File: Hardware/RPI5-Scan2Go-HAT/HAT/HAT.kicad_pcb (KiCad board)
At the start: 2 copper layers, 76 x 96.5 mm, 39 parts, among them J1 RPi_GPIO, J10 Conn_01x02_Socket, J12 Conn_01x02_Socket, J13 Conn_01x02_Socket, J14 Conn_01x02_Socket, J15 Jack-DC 5V, J18 Conn_01x02_Socket, J19 Conn_01x02_Socket, J2 Conn_01x04_Socket, J20 Conn_01x05_Socket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

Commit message: minor improvements
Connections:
- J8 pad 1: /PICORST -> GND
- J8 pad 2: GND -> /PICORST
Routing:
- net /PICORST: track 42.0 -> 45.1 mm, vias 2 -> 3
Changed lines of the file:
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@@
 		(tags "TVS Diode (Uni-directional)")
 		(property "Reference" "D1"
-			(at 0 0 -90)
-			(layer "B.SilkS")
+			(at 0.1 2.9 90)
+			(layer "F.SilkS")
 			(effects
 				(font
-					(size 1.27 1.27)
-					(thickness 0.254)
+					(size 1 1)
+					(thickness 0.15)
 				)
-				(justify mirror)
 			)
 		)
@@
 			(remove_unused_layers no)
 			(roundrect_rratio 0.147059)
-			(net 5 "/PICORST")
+			(net 3 "GND")
 			(pinfunction "Pin_1")
 			(pintype "passive")
@@
 			(layers "*.Cu" "*.Mask")
 			(remove_unused_layers no)
-			(net 3 "GND")
+			(net 5 "/PICORST")
 			(pinfunction "Pin_2")
 			(pintype "passive")
@@
 		(tags "capacitor handsolder")
 		(property "Reference" "C1"
-			(at 0 -1.85 -180)
-			(layer "B.SilkS")
+			(at 0 -1.85 180)
+			(layer "F.SilkS")
 			(effects
 				(font
@@
 					(thickness 0.15)
 				)
-				(justify mirror)
 			)
 		)
@@
 		(tags "fuse handsolder")
 		(property "Reference" "F1"
-			(at 0 2.3 -270)
-			(layer "B.SilkS")
+			(at 0 2.3 270)
+			(layer "F.SilkS")
 			(effects
 				(font
@@
 					(thickness 0.15)
 				)
-				(justify mirror)
 			)
 		)
@@
 			(layer "F.SilkS")
 		)
-		(fp_poly
-			(pts
-				(xy 3.7 -20.2) (xy -3.7 -20.2) (xy -3.7 -24.9) (xy 3.7 -24.9)
-			)
-			(stroke
-				(width 0.1)
-				(type solid)
-			)
-			(fill solid)
-			(layer "Dwgs.User")
-		)
-		(fp_poly
-			(pts
-				(xy -1.5 -16.5) (xy -3.5 -16.5) (xy -3.5 -18.5) (xy -1.5 -18.5)
-			)
+		(fp_rect
+			(start -3.4544 -25.5016)
+			(end 3.7084 -20.4724)
 			(stroke
 				(width 0.1)
-				(type solid)
+				(type default)
 			)
-			(fill solid)
-			(layer "Dwgs.User")
+			(fill none)
+			(layer "F.SilkS")
+			(net 9)
 		)
-		(fp_poly
-			(pts
-				(xy -1.5 -14) (xy -3.5 -14) (xy -3.5 -16) (xy -1.5 -16)
-			)
+		(fp_rect
+			(start -1.6764 -25.0952)
+			(end -1.016 -24.2316)
 			(stroke
 				(width 0.1)
-				(type solid)
+				(type default)
 			)
-			(fill solid)
-			(layer "Dwgs.User")
+			(fill none)
+			(layer "F.SilkS")
+			(net 9)
 		)
-		(fp_poly
-			(pts
-				(xy -1.5 -11.5) (xy -3.5 -11.5) (xy -3.5 -13.5) (xy -1.5 -13.5)
-			)
+		(fp_rect
+			(start 1.3716 -25.0444)
+			(end 2.032 -24.1808)
 			(stroke
 				(width 0.1)
-				(type solid)
+				(type default)
 			)
-			(fill solid)
-			(layer "Dwgs.User")
+			(fill none)
+			(layer "F.SilkS")
 		)
 		(fp_line
@@
 			(layer "F.Fab")
 		)
-		(fp_text user "PICO"
-			(at -3.1 -1 90)
+		(fp_text user "USB"
+			(at -2.9464 -20.9296 90)
 			(unlocked yes)
 			(layer "F.SilkS")
@@
 				(font
 					(size 2 2)
-					(thickness 0.25)
+					(thickness 0.2)
 				)
 				(justify left bottom)
@@
 				(offset 0.31 -0.0694)
 			)
-			(layers "F.Cu" "F.Paste")
+			(layers "F.Cu" "F.Mask")
 			(net 80 "unconnected-(U1-SWCLK-Pad41)")
 			(pinfunction "SWCLK")
@@
 		(tags "LED RGB NeoPixel PLCC-4 5050")
 		(property "Reference" "D2"
-			(at 0 -3.5 -180)
-			(layer "B.SilkS")
+			(at 0 -3.5 180)
+			(layer "F.SilkS")
 			(effects
 				(font
@@
 					(thickness 0.15)
 				)
-				(justify mirror)
 			)
 		)
@@
 	)
 	(gr_rect
-		(start 93.2524 115.9166)
+		(start 93.2524 115.8166)
 		(end 107.7558 128.712)
 		(stroke
@@
 	)
 	(via
-		(at 114.1 108.3)
+		(at 113.9 107.95)
 		(size 0.6)
 		(drill 0.3)
@@
 	)
 	(via
-		(at 114.9 121.4)
+		(at 114.95 121.7)
 		(size 0.6)
 		(drill 0.3)
@@
 	)
 	(via
-		(at 122 114.8)
+		(at 122.05 114.9)
 		(size 0.6)
 		(drill 0.3)
@@
 	)
 	(via
-		(at 95.5 115.8)
+		(at 94.05 115.4)
 		(size 0.6)
 		(drill 0.3)
@@
 	)
 	(via
-		(at 101.8 115.7)
+		(at 107.4 115.45)
 		(size 0.6)
 		(drill 0.3)
@@
 	)
 	(via
-		(at 109.3 112.2)
+		(at 109.05 111.5)
 		(size 0.6)
 		(drill 0.3)
@@
 	)
 	(via
-		(at 111.5 115.7)
+		(at 111.5 115.3)
 		(size 0.6)
 		(drill 0.3)
@@
 	)
 	(via
-		(at 96.7 121.1)
+		(at 101.1 120.7)
 		(size 0.6)
 		(drill 0.3)
@@
 	)
 	(via
-		(at 112.8 108.3)
+		(at 111.65 107.95)
 		(size 0.6)
 		(drill 0.3)
@@
 	)
 	(via
-		(at 103.6 121.2)
+		(at 103.05 122.65)
 		(size 0.6)
 		(drill 0.3)
@@
 	)
 	(segment
+		(start 112.575 115.875)
+		(end 114.678 117.978)
+		(width 0.25)
+		(layer "F.Cu")
+		(net 5)
+	)
+	(segment
 		(start 103.1112 87.3862)
 		(end 104.7832 87.3862)
@@
 	)
 	(segment
+		(start 112.225 115.875)
+		(end 112.575 115.875)
+		(width 0.25)
+		(layer "F.Cu")
+		(net 5)
+	)
+	(segment
 		(start 100.327 82.8652)
 		(end 101.625 84.1632)
@@
 		(net 5)
 	)
+	(segment
+		(start 114.678 117.978)
+		(end 114.678 118.933)
+		(width 0.25)
+		(layer "F.Cu")
+		(net 5)
+	)
+	(via
+		(at 112.225 115.875)
+		(size 0.6)
+		(drill 0.3)
+		(layers "F.Cu" "B.Cu")
+		(net 5)
+	)
 	(via
 		(at 107.4 101.3)
@@
 	)
 	(segment
+		(start 112.225 115.875)
+		(end 112.175 115.925)
+		(width 0.25)
+		(layer "B.Cu")
+		(net 5)
+	)
+	(segment
+		(start 107.3918 101.3082)
+		(end 107.4 101.3)
+		(width 0.25)
+		(layer "B.Cu")
+		(net 5)
+	)
+	(segment
 		(start 107.4 94)
 		(end 106.0268 92.6268)
@@
 	)
 	(segment
-		(start 107.3918 114.1468)
-		(end 107.3918 101.3082)
+		(start 109.17 115.925)
+		(end 107.3918 114.1468)
 		(width 0.25)
 		(layer "B.Cu")
@@
 	)
 	(segment
-		(start 106.0268 92.6268)
-		(end 106.0268 88.6298)
+		(start 107.3918 114.1468)
+		(end 107.3918 101.3082)
 		(width 0.25)
 		(layer "B.Cu")
@@
 	)
 	(segment
-		(start 107.3918 101.3082)
-		(end 107.4 101.3)
+		(start 112.175 115.925)
+		(end 109.17 115.925)
 		(width 0.25)
 		(layer "B.Cu")
@@
 	)
 	(segment
-		(start 112.178 118.933)
-		(end 107.3918 114.1468)
+		(start 106.0268 92.6268)
+		(end 106.0268 88.6298)
 		(width 0.25)
 		(layer "B.Cu")
@@
 	)
 	(zone
-		(net 1)
-		(net_name "Net-(D2-DIN)")
-		(layer "F.Cu")
-		(name "$teardrop_padvia$")
-		(hatch full 0.1)
-		(priority 30000)
-		(attr
-			(teardrop
-				(type padvia)
-			)
-		)
-		(connect_pads yes
-			(clearance 0)
-		)
-		(min_thickness 0.0254)
-		(filled_areas_thickness no)
-		(fill yes
-			(thermal_gap 0.5)
-			(thermal_bridge_width 0.5)
-			(island_removal_mode 1)
-			(island_area_min 10)
-		)
-		(polygon
-			(pts
-				(xy 71.2783 100.9238) (xy 71.2783 101.1738) (xy 71.763495 101.325964) (xy 71.8793 101.0488) (xy 71.763495 100.771636)
-			)
-		)
-	)
-	(zone
 		(net 3)
 		(net_name "GND")
@@
 	)
 	(zone
-		(net 3)
-		(net_name "GND")
-		(layer "B.Cu")
-		(hatch edge 0.5)
-		(priority 1)
-		(connect_pads
-			(clearance 0.3)
+		(net 1)
+		(net_name "Net-(D2-DIN)")
+		(layer "F.Cu")
+		(name "$teardrop_padvia$")
+		(hatch full 0.1)
+		(priority 30000)
+		(attr
+			(teardrop
+				(type padvia)
+			)
 		)
-		(min_thickness 0.25)
+		(connect_pads yes
+			(clearance 0)
+		)
+		(min_thickness 0.0254)
 		(filled_areas_thickness no)
 		(fill yes
 			(thermal_gap 0.5)
 			(thermal_bridge_width 0.5)
+			(island_removal_mode 1)
+			(island_area_min 10)
 		)
 		(polygon
 			(pts
-				(xy 59.775 37.85) (xy 141.375 37.75) (xy 142.275 136.95) (xy 59.475 137.75)
+				(xy 71.2783 100.9238) (xy 71.2783 101.1738) (xy 71.763495 101.325964) (xy 71.8793 101.0488) (xy 71.763495 100.771636)
 			)
 		)
@@
 			)
 		)
+	)
+	(zone
+		(net 3)
+		(net_name "GND")
+		(layer "B.Cu")
+		(hatch edge 0.5)
+		(priority 1)
+		(connect_pads
+			(clearance 0.3)
+		)
+		(min_thickness 0.25)
+		(filled_areas_thickness no)
+		(fill yes
+			(thermal_gap 0.5)
+			(thermal_bridge_width 0.5)
+		)
+		(polygon
+			(pts
+				(xy 59.775 37.85) (xy 141.375 37.75) (xy 142.275 136.95) (xy 59.475 137.75)
+			)
+		)

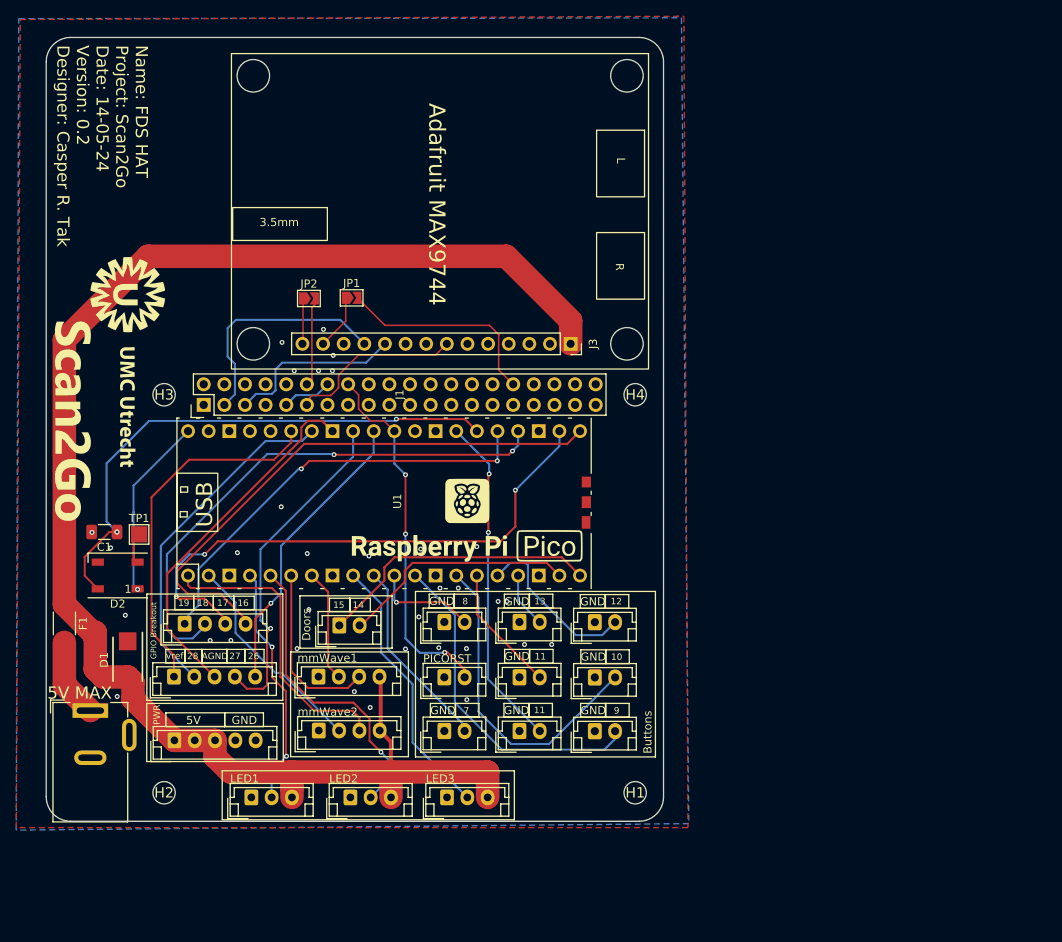
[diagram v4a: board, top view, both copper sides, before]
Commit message: V0.2 Finished
- added product ID
- via stitching
- improved silkscreen
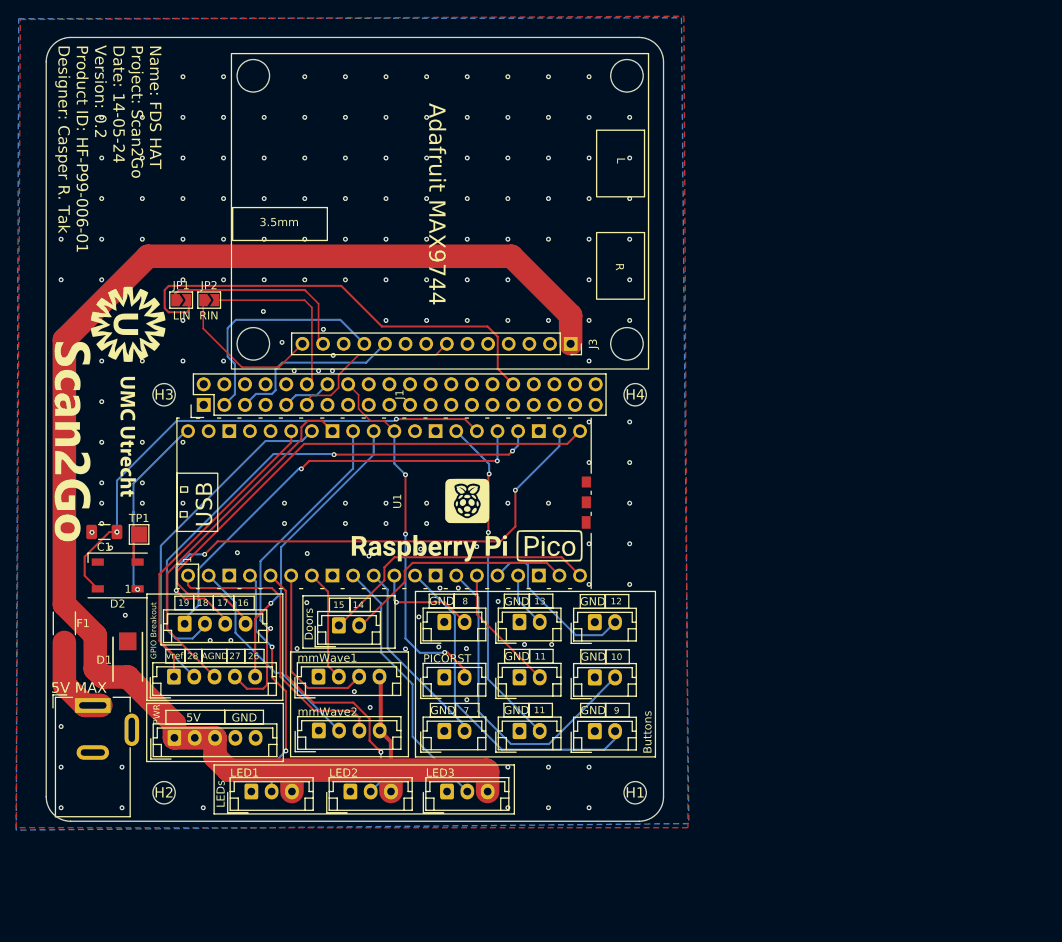
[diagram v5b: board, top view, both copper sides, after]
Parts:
- moved JP1 21.0 mm to (79.8, 72.5)
- moved JP2 12.3 mm to (83.2, 72.5)
- moved G*** 3.65 mm to (73.2, 83.8)
- moved G*** 2.52 mm to (65.8, 89.8)
- moved J4 0.72 mm to (88.4, 133.0)
- moved J5 0.72 mm to (100.6, 133.0)
- moved J6 0.72 mm to (112.5, 133.0)
- moved J15 0.71 mm to (68.9, 122.4)
- moved J21 0.31 mm to (79.0, 126.4)
- moved J18 0.06 mm to (99.2, 112.5)
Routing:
- net Net-(J1-BCM12_PWM0): track 26.1 -> 57.2 mm
- net Net-(J3-LIN): track 6.82 -> 25.1 mm
- net Net-(J3-RIN): track 5.61 -> 18.9 mm
- net Net-(J1-BCM18_PCM_C): track 11.0 -> 22.0 mm
- net Net-(J20-Pin_1): track 44.6 -> 37.7 mm
- net Net-(D2-DIN): track 67.3 -> 64.2 mm
- net +5V: track 192.9 -> 190.9 mm
- net Net-(J5-Pin_2): track 37.3 -> 35.6 mm
- net Net-(F1-Pad1): track 9.72 -> 10.8 mm
- net Net-(J4-Pin_2): track 29.9 -> 29.2 mm
- net Net-(J6-Pin_2): track 33.1 -> 32.4 mm
- net GND: vias 33 -> 165
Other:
- board text added: "LEDs"
- board text added: "LIN"
- board text added: "Name: FDS HAT Project: Scan2Go Date: 14-05-24 Version: 0.2 Product ID: HF-P99-006-01 Designer: Casper R. Tak"
- board text added: "RIN"
- board text removed: "Name: FDS HAT Project: Scan2Go Date: 14-05-24 Version: 0.2 Designer: Casper R. Tak"
